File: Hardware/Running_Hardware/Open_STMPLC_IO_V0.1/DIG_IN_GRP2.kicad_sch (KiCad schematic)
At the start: 54 parts, among them J16 Screw_Terminal_01x02, J17 Screw_Terminal_01x02, J18 Screw_Terminal_01x02, J19 Screw_Terminal_01x02, J20 Screw_Terminal_01x02, J3 Screw_Terminal_01x02, U12 6N137, U20 6N137, U21 6N137, U22 6N137, U23 6N137, U24 6N137

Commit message: Analog input section
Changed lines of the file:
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@@
 			(effects
 				(font
-					(size 1.27 1.27)
+					(size 1 1)
 				)
 				(justify left)
@@
 			(effects
 				(font
-					(size 1.27 1.27)
+					(size 1 1)
 				)
 				(justify left)
@@
 			(effects
 				(font
-					(size 1.27 1.27)
+					(size 1 1)
 				)
 			)
@@
 			(effects
 				(font
-					(size 1.27 1.27)
+					(size 1 1)
 				)
 			)
@@
 			(effects
 				(font
-					(size 1.27 1.27)
+					(size 1 1)
 				)
 			)
@@
 			(effects
 				(font
-					(size 1.27 1.27)
+					(size 1 1)
 				)
 			)
@@
 			(effects
 				(font
-					(size 1.27 1.27)
+					(size 1 1)
 				)
 			)
@@
 			(effects
 				(font
-					(size 1.27 1.27)
+					(size 1 1)
 				)
 			)
@@
 			(effects
 				(font
-					(size 1.27 1.27)
+					(size 1 1)
 				)
 				(justify left)
@@
 			(effects
 				(font
-					(size 1.27 1.27)
+					(size 1 1)
 				)
 				(justify left)
@@
 			(effects
 				(font
-					(size 1.27 1.27)
+					(size 1 1)
 				)
 			)
@@
 			(effects
 				(font
-					(size 1.27 1.27)
+					(size 1 1)
 				)
 			)
@@
 			(effects
 				(font
-					(size 1.27 1.27)
+					(size 1 1)
 				)
 				(justify left)
@@
 			(effects
 				(font
-					(size 1.27 1.27)
+					(size 1 1)
 				)
 				(justify left)
@@
 			(effects
 				(font
-					(size 1.27 1.27)
+					(size 1 1)
 				)
 				(justify left)
@@
 			(effects
 				(font
-					(size 1.27 1.27)
+					(size 1 1)
 				)
 				(justify left)
@@
 			(effects
 				(font
-					(size 1.27 1.27)
+					(size 1 1)
 				)
 				(justify left)
@@
 			(effects
 				(font
-					(size 1.27 1.27)
+					(size 1 1)
 				)
 				(justify left)
@@
 			(effects
 				(font
-					(size 1.27 1.27)
+					(size 1 1)
 				)
 			)
@@
 			(effects
 				(font
-					(size 1.27 1.27)
+					(size 1 1)
 				)
 			)
@@
 			(effects
 				(font
-					(size 1.27 1.27)
+					(size 1 1)
 				)
 				(justify left)
@@
 			(effects
 				(font
-					(size 1.27 1.27)
+					(size 1 1)
 				)
 				(justify left)
@@
 			(effects
 				(font
-					(size 1.27 1.27)
+					(size 1 1)
 				)
 			)
@@
 			(effects
 				(font
-					(size 1.27 1.27)
+					(size 1 1)
 				)
 			)

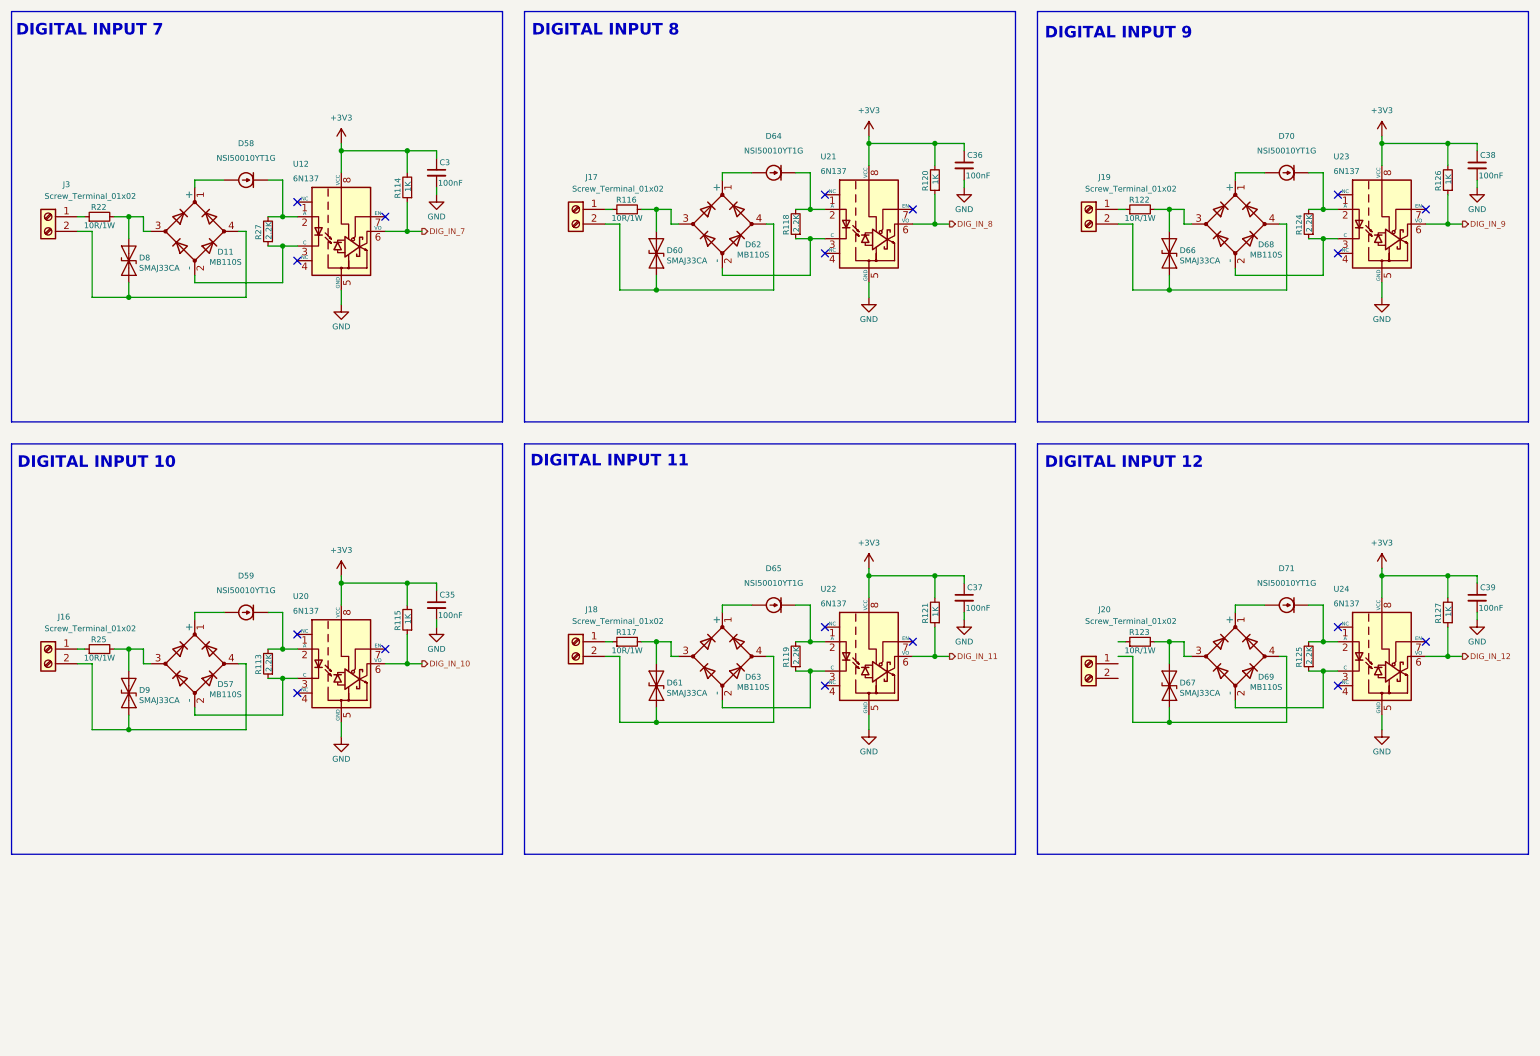
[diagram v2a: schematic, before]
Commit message: GSM Module add
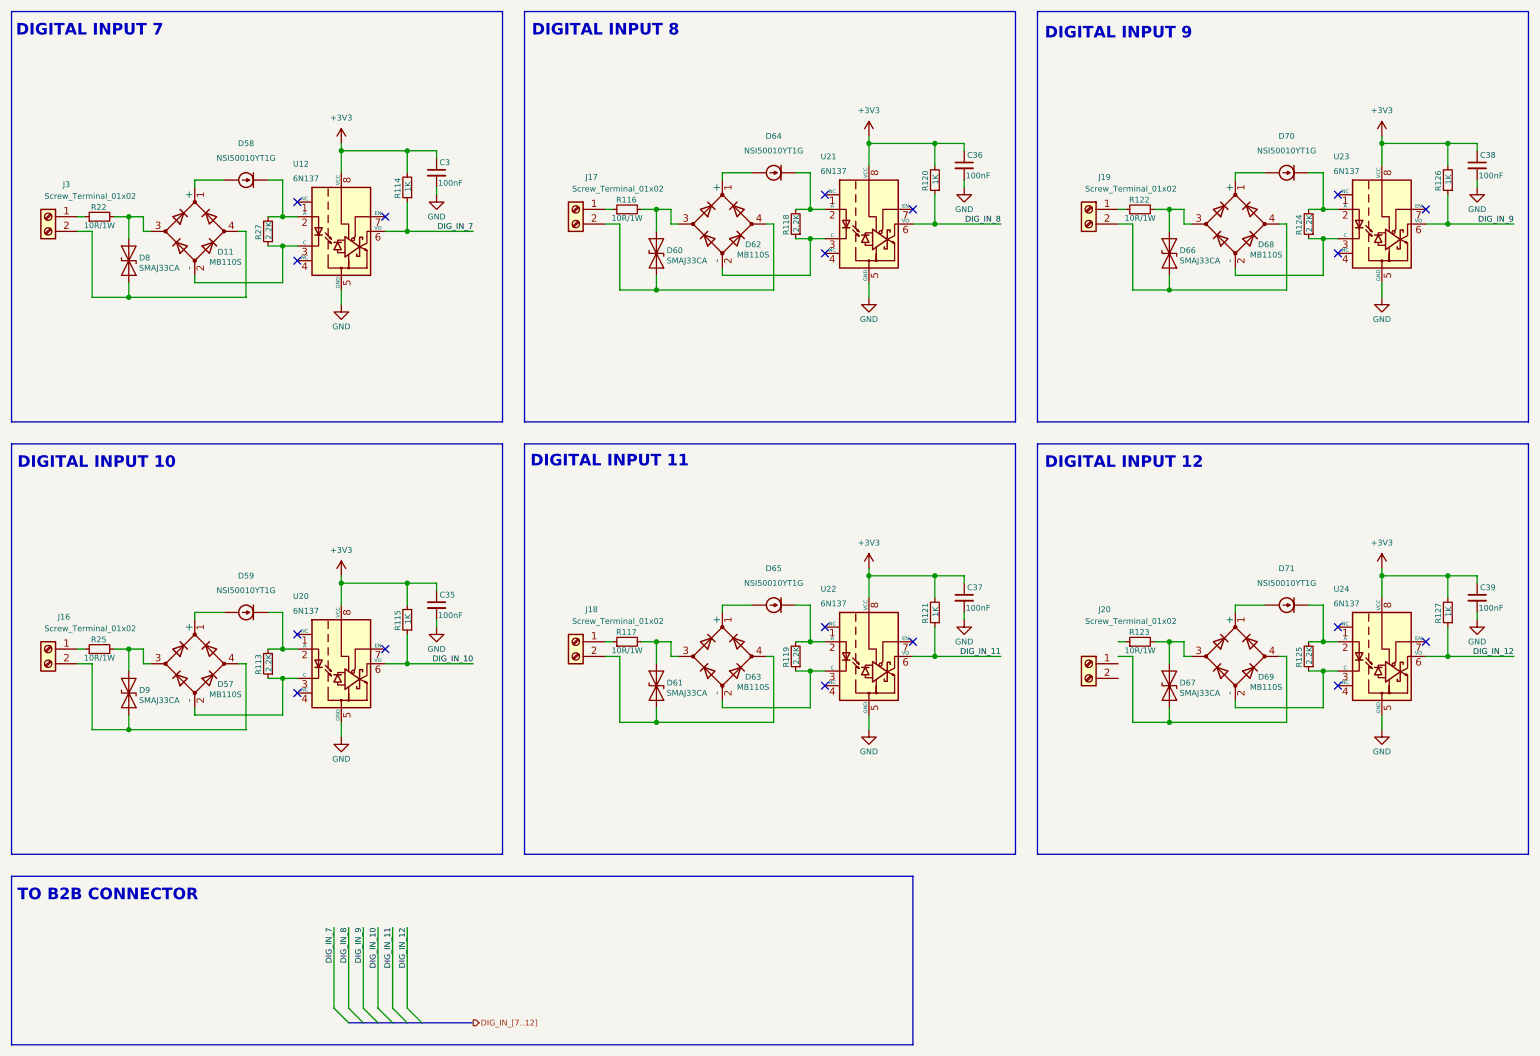
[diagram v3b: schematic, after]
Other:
- note added: "TO B2B CONNECTOR"
- title: (none) -> Open_PLC_IO

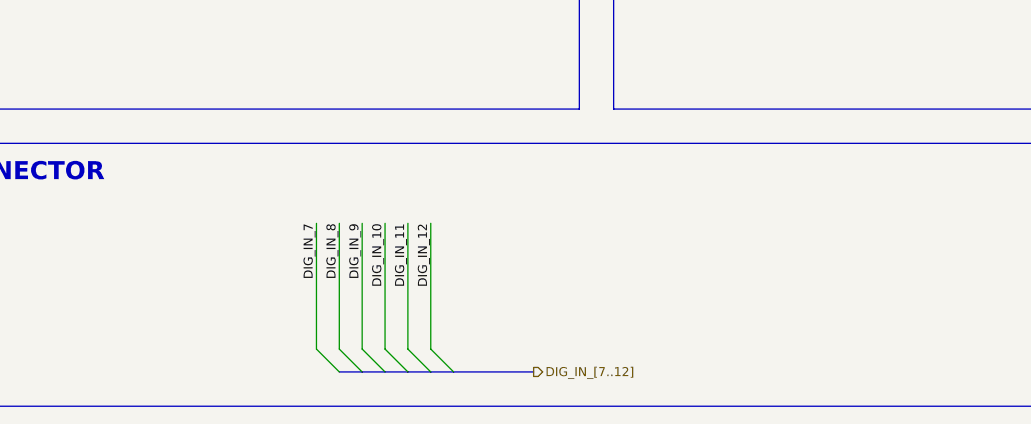
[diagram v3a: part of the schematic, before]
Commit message: Main PCB schematic changes V0.1
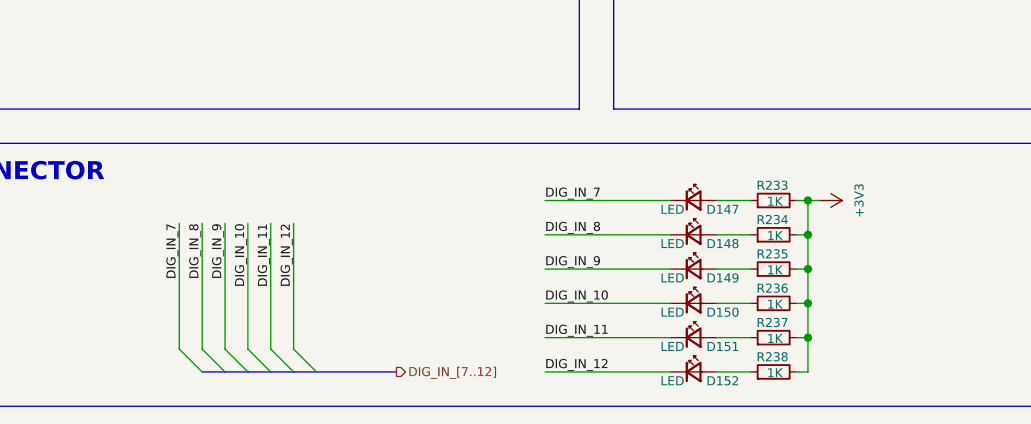
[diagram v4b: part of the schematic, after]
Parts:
- added D147, D148, D149, D150, D151, D152: LED, LED_SMD:LED_0603_1608Metric_Pad1.05x0.95mm_HandSolder, symbol Device:LED_Small
- added R233, R234, R235, R236, R237, R238: 1K, Resistor_SMD:R_0603_1608Metric_Pad0.98x0.95mm_HandSolder, symbol Device:R_Small
- C3, C35, C36, C37, C38, C39: footprint (none) -> Capacitor_SMD:C_0603_1608Metric_Pad1.08x0.95mm_HandSolder
- J16, J17, J18, J19, J20, J3: footprint (none) -> TerminalBlock_Phoenix:TerminalBlock_Phoenix_MKDS-1,5-2_1x02_P5.00mm_Horizontal
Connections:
- net +3V3: now also R233.2, R234.2, R235.2, R236.2, R237.2, R238.2
- net DIG_IN_10: now also D150.1 (K)
- net DIG_IN_11: now also D151.1 (K)
- net DIG_IN_12: now also D152.1 (K)
- net DIG_IN_7: now also D147.1 (K)
- net DIG_IN_8: now also D148.1 (K)
- net DIG_IN_9: now also D149.1 (K)
- new net: D150.2 (A), R236.1
- new net: D152.2 (A), R238.1
- new net: D147.2 (A), R233.1
- new net: D148.2 (A), R234.1
- new net: D151.2 (A), R237.1
- new net: D149.2 (A), R235.1
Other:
- title: Open_PLC_IO -> Open_STMPLC_IO

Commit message: New DXF update
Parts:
- J16, J17, J18, J19, J20, J3: footprint TerminalBlock_Phoenix:TerminalBlock_Phoenix_MKDS-1,5-2_1x02_P5.00mm_Horizontal -> TerminalBlock_Phoenix:TerminalBlock_Phoenix_MKDS-1-2-3.81_1x02_P3.81mm_Horizontal
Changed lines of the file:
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@@
 			)
 		)
-		(property "Footprint" "TerminalBlock_Phoenix:TerminalBlock_Phoenix_MKDS-1,5-2_1x02_P5.00mm_Horizontal"
+		(property "Footprint" "TerminalBlock_Phoenix:TerminalBlock_Phoenix_MKDS-1-2-3.81_1x02_P3.81mm_Horizontal"
 			(at 203.2 128.27 0)
 			(effects
@@
 			)
 		)
-		(property "Footprint" "TerminalBlock_Phoenix:TerminalBlock_Phoenix_MKDS-1,5-2_1x02_P5.00mm_Horizontal"
+		(property "Footprint" "TerminalBlock_Phoenix:TerminalBlock_Phoenix_MKDS-1-2-3.81_1x02_P3.81mm_Horizontal"
 			(at 114.3 124.46 0)
 			(effects
@@
 			)
 		)
-		(property "Footprint" "TerminalBlock_Phoenix:TerminalBlock_Phoenix_MKDS-1,5-2_1x02_P5.00mm_Horizontal"
+		(property "Footprint" "TerminalBlock_Phoenix:TerminalBlock_Phoenix_MKDS-1-2-3.81_1x02_P3.81mm_Horizontal"
 			(at 22.86 50.8 0)
 			(effects
@@
 			)
 		)
-		(property "Footprint" "TerminalBlock_Phoenix:TerminalBlock_Phoenix_MKDS-1,5-2_1x02_P5.00mm_Horizontal"
+		(property "Footprint" "TerminalBlock_Phoenix:TerminalBlock_Phoenix_MKDS-1-2-3.81_1x02_P3.81mm_Horizontal"
 			(at 114.3 49.53 0)
 			(effects
@@
 			)
 		)
-		(property "Footprint" "TerminalBlock_Phoenix:TerminalBlock_Phoenix_MKDS-1,5-2_1x02_P5.00mm_Horizontal"
+		(property "Footprint" "TerminalBlock_Phoenix:TerminalBlock_Phoenix_MKDS-1-2-3.81_1x02_P3.81mm_Horizontal"
 			(at 203.2 49.53 0)
 			(effects
@@
 			)
 		)
-		(property "Footprint" "TerminalBlock_Phoenix:TerminalBlock_Phoenix_MKDS-1,5-2_1x02_P5.00mm_Horizontal"
+		(property "Footprint" "TerminalBlock_Phoenix:TerminalBlock_Phoenix_MKDS-1-2-3.81_1x02_P3.81mm_Horizontal"
 			(at 22.86 125.73 0)
 			(effects

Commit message: Rule areas creation
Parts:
- removed J16, J17, J18, J19, J20, J3: Screw_Terminal_01x02, TerminalBlock_Phoenix:TerminalBlock_Phoenix_MKDS-1-2-3.81_1x02_P3.81mm_Horizontal, symbol Connector:Screw_Terminal_01x02
- added J3, J8: Screw_Terminal_01x04, TerminalBlock_Phoenix:TerminalBlock_Phoenix_MKDS-1-4-3.81_1x04_P3.81mm_Horizontal, symbol Connector:Screw_Terminal_01x04
- added R152, R153, R154, R155, R156, R157: 10R/1W, Resistor_SMD:R_0603_1608Metric_Pad0.98x0.95mm_HandSolder, symbol Device:R_Small
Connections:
- net at D57.4, D9.2 (A2): now also R157.2
- net at D67.2 (A2), D69.4: now also R156.2
- net at D60.2 (A2), D62.4: now also R152.2
- net at D61.2 (A2), D63.4: now also R155.2
- net at D66.2 (A2), D68.4: now also R153.2
- net DIG_IN_TERMINAL_8: now reaches R116.1
- net DIG_IN_TERMINAL_8: now also J3.2 (Pin_2)
- net DIG_IN_TERMINAL_12: now reaches R123.1
- net DIG_IN_TERMINAL_12: now also J8.1 (Pin_1)
- net DIG_IN_TERMINAL_11: now reaches R117.1
- net DIG_IN_TERMINAL_11: now also J8.2 (Pin_2)
- net DIG_IN_TERMINAL_7: now reaches R22.1
- net DIG_IN_TERMINAL_7: now also J3.3 (Pin_3)
- net at D11.4, D8.2 (A2): now also R154.2
- net DIG_IN_TERMINAL_9: now reaches R122.1
- net DIG_IN_TERMINAL_9: now also J3.1 (Pin_1)
- net DIG_IN_TERMINAL_10: now reaches R25.1
- net DIG_IN_TERMINAL_10: now also J8.3 (Pin_3)
- new net COMC: J3.4 (Pin_4), R152.1, R153.1, R154.1
- new net COMD: J8.4 (Pin_4), R155.1, R156.1, R157.1
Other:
- moved on the sheet: D147, D148, D149, D150, D151, D152, R233, R234, R235, R236, R237, R238

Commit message: IO board component grouping
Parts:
- R116, R117, R122, R123, R152, R153, R154, R155, R156, R157, R22, R25: footprint Resistor_SMD:R_0603_1608Metric_Pad0.98x0.95mm_HandSolder -> Resistor_SMD:R_2512_6332Metric_Pad1.40x3.35mm_HandSolder
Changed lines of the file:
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@@
 			)
 		)
-		(property "Footprint" "Resistor_SMD:R_0603_1608Metric_Pad0.98x0.95mm_HandSolder"
+		(property "Footprint" "Resistor_SMD:R_2512_6332Metric_Pad1.40x3.35mm_HandSolder"
 			(at 212.09 138.43 0)
 			(effects
@@
 			)
 		)
-		(property "Footprint" "Resistor_SMD:R_0603_1608Metric_Pad0.98x0.95mm_HandSolder"
+		(property "Footprint" "Resistor_SMD:R_2512_6332Metric_Pad1.40x3.35mm_HandSolder"
 			(at 123.19 49.53 0)
 			(effects
@@
 			)
 		)
-		(property "Footprint" "Resistor_SMD:R_0603_1608Metric_Pad0.98x0.95mm_HandSolder"
+		(property "Footprint" "Resistor_SMD:R_2512_6332Metric_Pad1.40x3.35mm_HandSolder"
 			(at 31.75 139.7 0)
 			(effects
@@
 			)
 		)
-		(property "Footprint" "Resistor_SMD:R_0603_1608Metric_Pad0.98x0.95mm_HandSolder"
+		(property "Footprint" "Resistor_SMD:R_2512_6332Metric_Pad1.40x3.35mm_HandSolder"
 			(at 212.09 124.46 0)
 			(effects
@@
 			)
 		)
-		(property "Footprint" "Resistor_SMD:R_0603_1608Metric_Pad0.98x0.95mm_HandSolder"
+		(property "Footprint" "Resistor_SMD:R_2512_6332Metric_Pad1.40x3.35mm_HandSolder"
 			(at 123.19 124.46 0)
 			(effects
@@
 			)
 		)
-		(property "Footprint" "Resistor_SMD:R_0603_1608Metric_Pad0.98x0.95mm_HandSolder"
+		(property "Footprint" "Resistor_SMD:R_2512_6332Metric_Pad1.40x3.35mm_HandSolder"
 			(at 31.75 50.8 0)
 			(effects
@@
 			)
 		)
-		(property "Footprint" "Resistor_SMD:R_0603_1608Metric_Pad0.98x0.95mm_HandSolder"
+		(property "Footprint" "Resistor_SMD:R_2512_6332Metric_Pad1.40x3.35mm_HandSolder"
 			(at 31.75 64.77 0)
 			(effects
@@
 			)
 		)
-		(property "Footprint" "Resistor_SMD:R_0603_1608Metric_Pad0.98x0.95mm_HandSolder"
+		(property "Footprint" "Resistor_SMD:R_2512_6332Metric_Pad1.40x3.35mm_HandSolder"
 			(at 212.09 49.53 0)
 			(effects
@@
 			)
 		)
-		(property "Footprint" "Resistor_SMD:R_0603_1608Metric_Pad0.98x0.95mm_HandSolder"
+		(property "Footprint" "Resistor_SMD:R_2512_6332Metric_Pad1.40x3.35mm_HandSolder"
 			(at 123.19 63.5 0)
 			(effects
@@
 			)
 		)
-		(property "Footprint" "Resistor_SMD:R_0603_1608Metric_Pad0.98x0.95mm_HandSolder"
+		(property "Footprint" "Resistor_SMD:R_2512_6332Metric_Pad1.40x3.35mm_HandSolder"
 			(at 212.09 63.5 0)
 			(effects
@@
 			)
 		)
-		(property "Footprint" "Resistor_SMD:R_0603_1608Metric_Pad0.98x0.95mm_HandSolder"
+		(property "Footprint" "Resistor_SMD:R_2512_6332Metric_Pad1.40x3.35mm_HandSolder"
 			(at 31.75 125.73 0)
 			(effects
@@
 			)
 		)
-		(property "Footprint" "Resistor_SMD:R_0603_1608Metric_Pad0.98x0.95mm_HandSolder"
+		(property "Footprint" "Resistor_SMD:R_2512_6332Metric_Pad1.40x3.35mm_HandSolder"
 			(at 123.19 138.43 0)
 			(effects

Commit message: IO board component placement
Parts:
- U12, U20, U21, U22, U23, U24: footprint Package_DIP:DIP-8_W7.62mm -> Package_DIP:SMDIP-8_W9.53mm_Clearance8mm
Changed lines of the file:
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@@
 			)
 		)
-		(property "Footprint" "Package_DIP:DIP-8_W7.62mm"
+		(property "Footprint" "Package_DIP:SMDIP-8_W9.53mm_Clearance8mm"
 			(at 165.1 64.77 0)
 			(effects
@@
 			)
 		)
-		(property "Footprint" "Package_DIP:DIP-8_W7.62mm"
+		(property "Footprint" "Package_DIP:SMDIP-8_W9.53mm_Clearance8mm"
 			(at 254 64.77 0)
 			(effects
@@
 			)
 		)
-		(property "Footprint" "Package_DIP:DIP-8_W7.62mm"
+		(property "Footprint" "Package_DIP:SMDIP-8_W9.53mm_Clearance8mm"
 			(at 73.66 66.04 0)
 			(effects
@@
 			)
 		)
-		(property "Footprint" "Package_DIP:DIP-8_W7.62mm"
+		(property "Footprint" "Package_DIP:SMDIP-8_W9.53mm_Clearance8mm"
 			(at 254 139.7 0)
 			(effects
@@
 			)
 		)
-		(property "Footprint" "Package_DIP:DIP-8_W7.62mm"
+		(property "Footprint" "Package_DIP:SMDIP-8_W9.53mm_Clearance8mm"
 			(at 73.66 140.97 0)
 			(effects
@@
 			)
 		)
-		(property "Footprint" "Package_DIP:DIP-8_W7.62mm"
+		(property "Footprint" "Package_DIP:SMDIP-8_W9.53mm_Clearance8mm"
 			(at 165.1 139.7 0)
 			(effects
